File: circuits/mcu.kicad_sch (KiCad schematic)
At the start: 14 parts, among them J1 USB Mini-B, J2 UART->Pi, U10 USBLC6, U11 AP2112K-3.3, U9 ESP32-S3-WROOM-1

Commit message: chore(circuits): update laser controller release artifacts
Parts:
- removed U9: ESP32-S3-WROOM-1, RF_Module:ESP32-S3-WROOM-1, symbol Espressif:ESP32-S3-WROOM-1
- added C29: 1uF, Capacitor_SMD:C_0402_1005Metric_Pad0.74x0.62mm_HandSolder, symbol viv:C_V
- U9: renamed from C29; value 1uF -> ESP32-S3-WROOM-1; footprint Capacitor_SMD:C_0402_1005Metric_Pad0.74x0.62mm_HandSolder -> RF_Module:ESP32-S3-WROOM-1; symbol viv:C_V -> Espressif:ESP32-S3-WROOM-1; LCSC C52923 -> C2913199; Part Number CL05A105KA5NQNC -> ESP32-S3-WROOM-1-N16R8
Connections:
- net +3V3: now also U9.2 (3V3)
- net +5V: now also C29.1; no longer U9.1
- net CONVST: now also U9.10 (GPIO17/U1TXD/ADC2_CH6)
- net ESP_BOOT: now also U9.27 (GPIO0/BOOT)
- net ESP_EN: now also U9.3 (EN)
- net ESP_RX: now also U9.36 (U0RXD/GPIO44/CLK_OUT2)
- net ESP_TX: now also U9.37 (U0TXD/GPIO43/CLK_OUT1)
- net GND: now also U9.1 (GND), U9.40 (GND), U9.41 (GND), C29.2; no longer U9.2
- net ISENSE1: now also U9.4 (GPIO4/TOUCH4/ADC1_CH3)
- net ISENSE2: now also U9.5 (GPIO5/TOUCH5/ADC1_CH4)
- net ISENSE3: now also U9.6 (GPIO6/TOUCH6/ADC1_CH5)
- net ISENSE4: now also U9.7 (GPIO7/TOUCH7/ADC1_CH6)
- net MPD1: now also U9.38 (GPIO2/TOUCH2/ADC1_CH1)
- net MPD2: now also U9.39 (GPIO1/TOUCH1/ADC1_CH0)
- net MPD3: now also U9.12 (GPIO8/TOUCH8/ADC1_CH7/SUBSPICS1)
- net MPD4: now also U9.17 (GPIO9/TOUCH9/ADC1_CH8/FSPIHD/SUBSPIHD)
- net PWM1: now also U9.9 (GPIO16/U0CTS/ADC2_CH5/XTAL_32K_N)
- net PWM2: now also U9.31 (GPIO38/FSPIWP/SUBSPIWP)
- net PWM3: now also U9.21 (GPIO13/TOUCH13/ADC2_CH2/FSPIQ/FSPIIO7/SUBSPIQ)
- net PWM4: now also U9.22 (GPIO14/TOUCH14/ADC2_CH3/FSPIWP/FSPIDQS/SUBSPIWP)
- net USB_DM: now also U9.13 (GPIO19/U1RTS/ADC2_CH8/CLK_OUT2/USB_D-)
- net USB_DP: now also U9.14 (GPIO20/U1CTS/ADC2_CH9/CLK_OUT1/USB_D+)

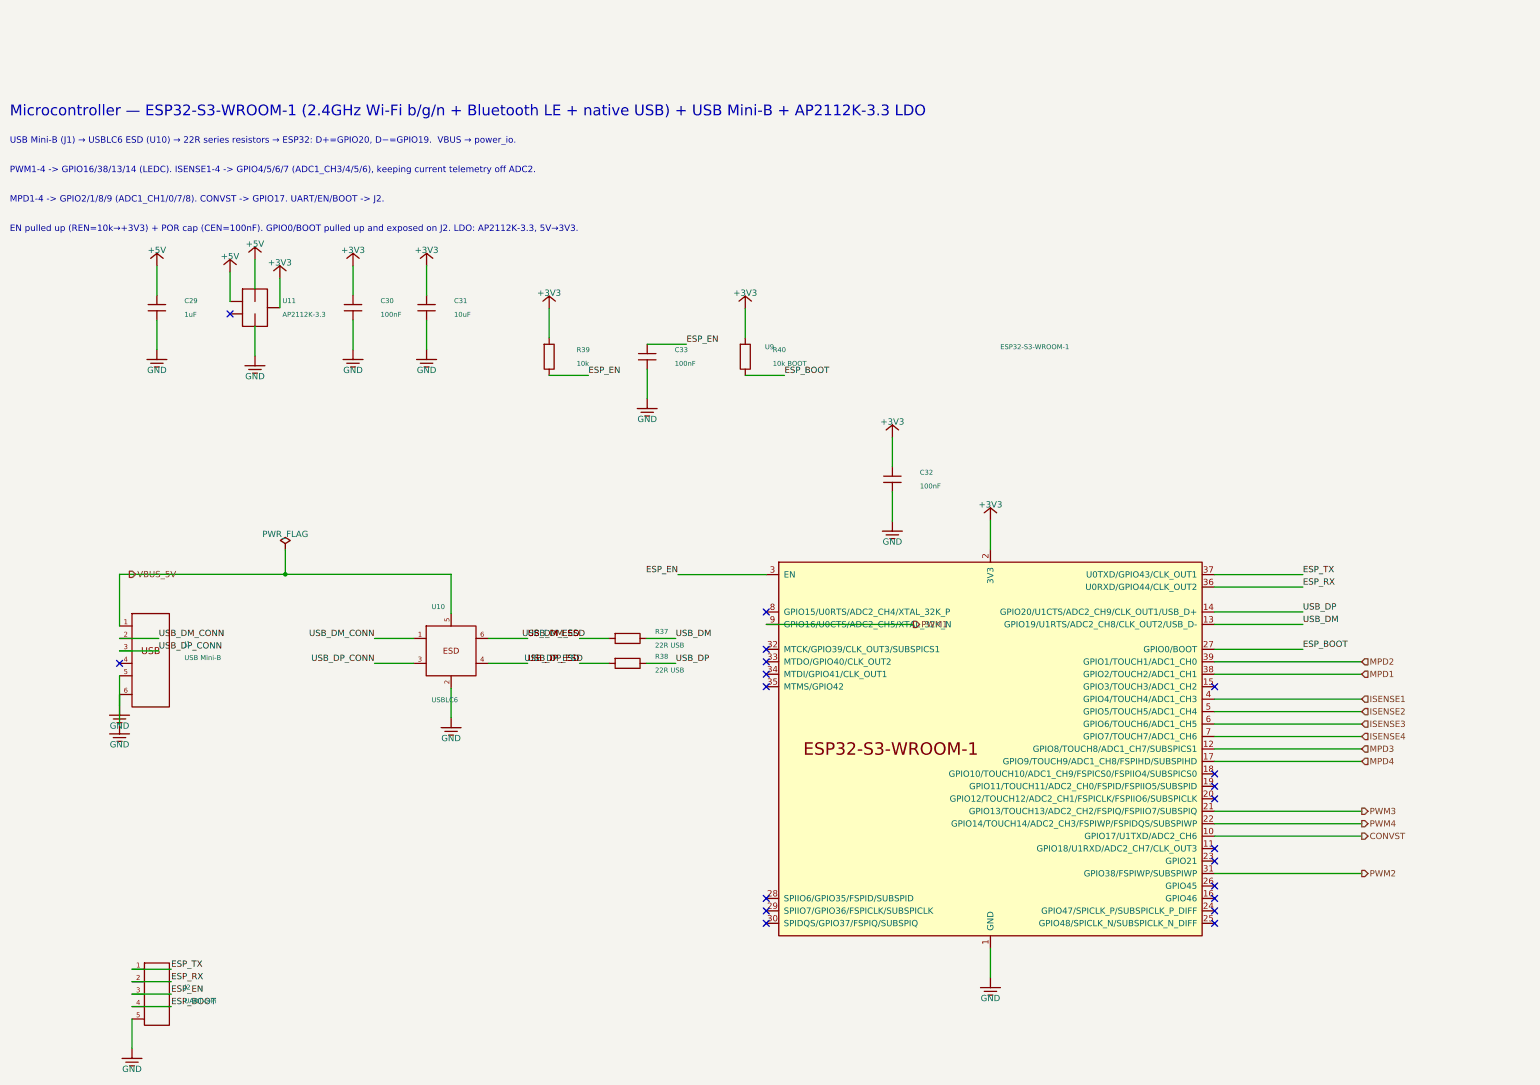
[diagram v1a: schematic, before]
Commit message: fix(circuits): import mcu sheet and laser footprints
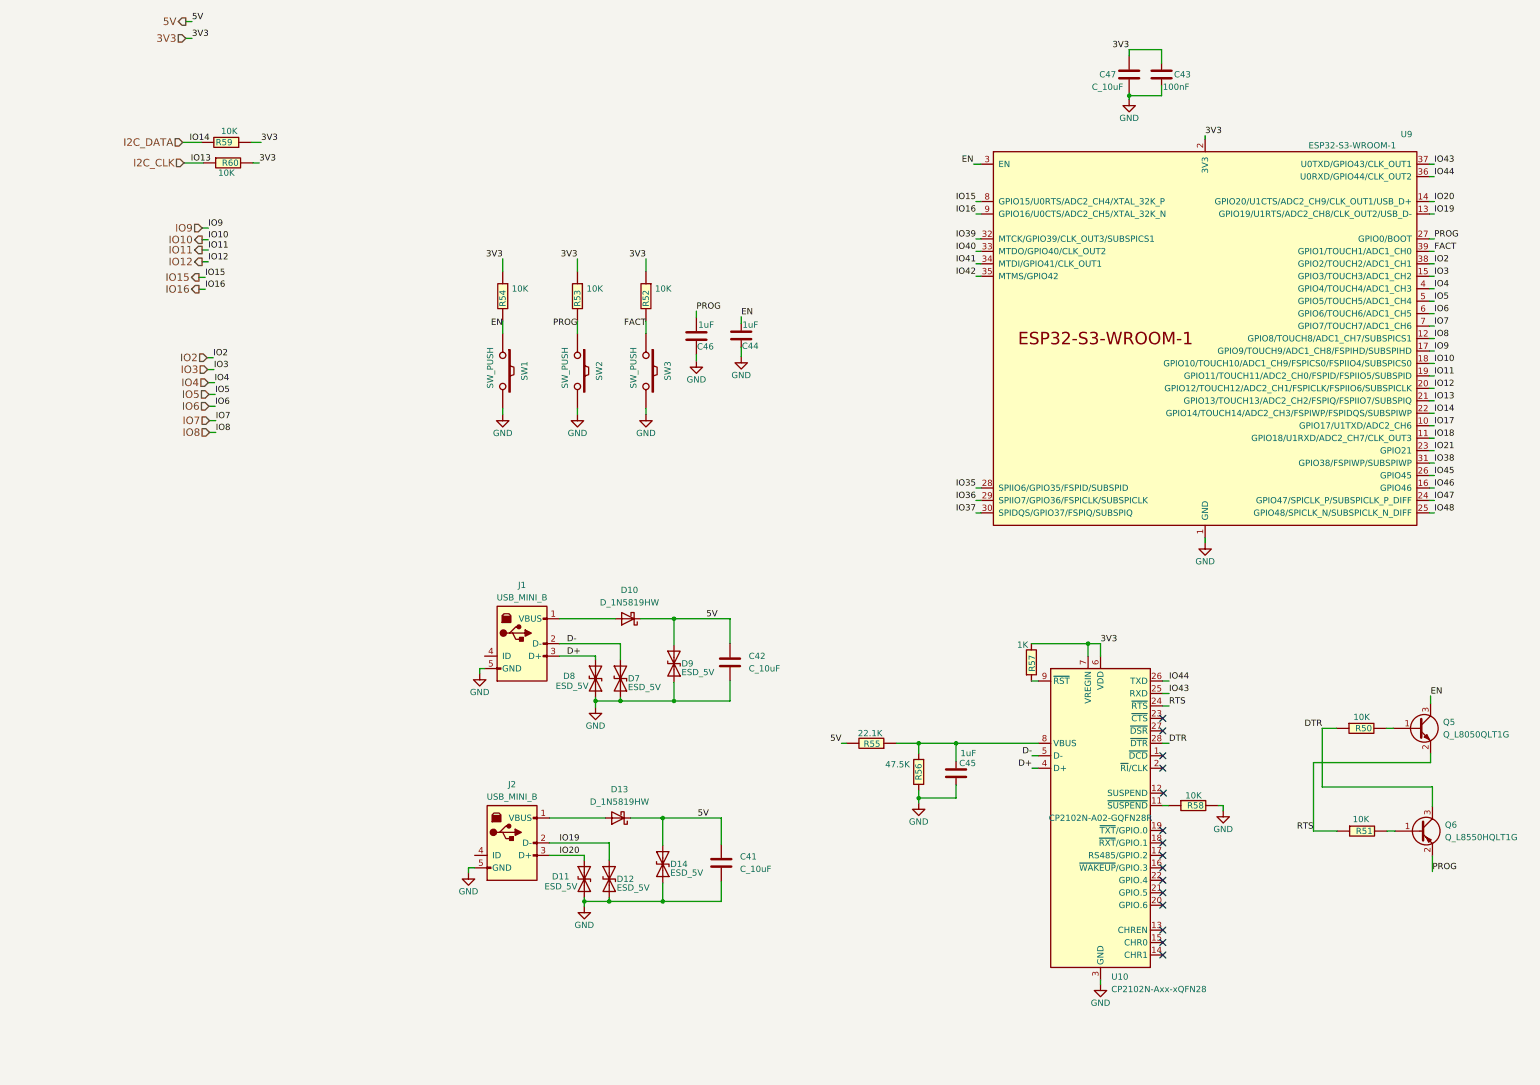
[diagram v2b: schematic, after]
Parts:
- removed C29: 1uF, Capacitor_SMD:C_0402_1005Metric_Pad0.74x0.62mm_HandSolder, symbol viv:C_V
- removed C30, C32, C33: 100nF, Capacitor_SMD:C_0402_1005Metric_Pad0.74x0.62mm_HandSolder, symbol viv:C_V
- removed C31: 10uF, Capacitor_SMD:C_0805_2012Metric_Pad1.18x1.45mm_HandSolder, symbol viv:C_V
- removed J1: USB Mini-B, Connector_USB:USB_Mini-B_Wuerth_65100516121_Horizontal, symbol viv:USB_MINIB
- removed J2: UART->Pi, Connector_PinHeader_2.54mm:PinHeader_1x05_P2.54mm_Vertical, symbol viv:CONN5
- removed R37, R38: 22R USB, Resistor_SMD:R_0603_1608Metric_Pad0.98x0.95mm_HandSolder, symbol viv:R_H
- removed R39: 10k, Resistor_SMD:R_0603_1608Metric_Pad0.98x0.95mm_HandSolder, symbol viv:R_V
- removed R40: 10k BOOT, Resistor_SMD:R_0603_1608Metric_Pad0.98x0.95mm_HandSolder, symbol viv:R_V
- removed U10: USBLC6, Package_TO_SOT_SMD:SOT-23-6, symbol viv:ESD_USB
- removed U11: AP2112K-3.3, Package_TO_SOT_SMD:SOT-23-5, symbol viv:LDO5
- added C41, C42: C_10uF, Capacitor_SMD:C_0805_2012Metric_Pad1.18x1.45mm_HandSolder, symbol open_automation:C_10uF
- added C43: 100nF, Capacitor_SMD:C_0402_1005Metric_Pad0.74x0.62mm_HandSolder, symbol open_automation:C_100nF_0402
- added C44, C45: 1uF, Capacitor_SMD:C_0402_1005Metric_Pad0.74x0.62mm_HandSolder, symbol open_automation:C_1uF
- added C46: 1uF, Capacitor_SMD:C_0402_1005Metric_Pad0.74x0.62mm_HandSolder, symbol Open_Automation:C_1uF
- added C47: C_10uF, Capacitor_SMD:C_0805_2012Metric_Pad1.18x1.45mm_HandSolder, symbol Open_Automation:C_10uF
- added D10, D13: D_1N5819HW, Diode_SMD:D_SOD-123, symbol open_automation:D_1N5819HW
- added D11, D12, D14, D7, D8, D9: ESD_5V, Diode_SMD:D_SOD-523, symbol open_automation:D_ESD9B5.0ST5G
- added J1, J2: USB_MINI_B, Connector_USB:USB_Mini-B_Wuerth_65100516121_Horizontal, symbol open_automation:USB_MINI_B_SMD
- added Q5: Q_L8050QLT1G, Package_TO_SOT_SMD:SOT-23, symbol open_automation:Q_L8050QLT1G
- added Q6: Q_L8550HQLT1G, Package_TO_SOT_SMD:SOT-23, symbol open_automation:Q_L8550HQLT1G
- added R50, R51, R52, R53, R54, R58, R59, R60: 10K, Resistor_SMD:R_0402_1005Metric_Pad0.72x0.64mm_HandSolder, symbol Open_Automation:R_10K_0402
- added R55: 22.1K, Resistor_SMD:R_0402_1005Metric_Pad0.72x0.64mm_HandSolder, symbol open_automation:R_22.1K_0402
- added R56: 47.5K, Resistor_SMD:R_0603_1608Metric_Pad0.98x0.95mm_HandSolder, symbol open_automation:R_47.5k
- added R57: 1K, Resistor_SMD:R_0402_1005Metric_Pad0.72x0.64mm_HandSolder, symbol open_automation:R_1K_0402
- added SW1, SW2, SW3: SW_PUSH, Button_Switch_SMD:SW_SPST_PTS645, symbol open-dash-daughterboard-rescue:SW_PUSH-Open_Automation
- added U10: CP2102N-Axx-xQFN28, Package_DFN_QFN:QFN-28-1EP_5x5mm_P0.5mm_EP3.35x3.35mm, symbol Interface_USB:CP2102N-Axx-xQFN28
- U9: footprint RF_Module:ESP32-S3-WROOM-1 -> Espressif:ESP32-S3-WROOM-1; Part Number ESP32-S3-WROOM-1-N16R8 -> ESP32-S3-WROOM-1-N16
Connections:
- net GND: now also C41.2, C42.2, C43.2, C44.2, C45.2, C46.2, C47.2, D11.1 (A1), D12.1 (A1), D14.1 (A1), D7.1 (A1), D8.1 (A1), D9.1 (A1), J1.5 (GND), J2.5 (GND), R56.1, R58.2, SW1.2, SW2.2, SW3.2, U10.29 (GND), U10.3 (GND)
- net IO18: now reaches U9.11 (GPIO18/U1RXD/ADC2_CH7/CLK_OUT3)
- net IO3: now reaches U9.15 (GPIO3/TOUCH3/ADC1_CH2)
- net IO46: now reaches U9.16 (GPIO46)
- net IO10: now reaches U9.18 (GPIO10/TOUCH10/ADC1_CH9/FSPICS0/FSPIIO4/SUBSPICS0)
- net IO11: now reaches U9.19 (GPIO11/TOUCH11/ADC2_CH0/FSPID/FSPIIO5/SUBSPID)
- net IO12: now reaches U9.20 (GPIO12/TOUCH12/ADC2_CH1/FSPICLK/FSPIIO6/SUBSPICLK)
- net IO21: now reaches U9.23 (GPIO21)
- net IO47: now reaches U9.24 (GPIO47/SPICLK_P/SUBSPICLK_P_DIFF)
- net IO48: now reaches U9.25 (GPIO48/SPICLK_N/SUBSPICLK_N_DIFF)
- net IO45: now reaches U9.26 (GPIO45)
- net IO35: now reaches U9.28 (SPIIO6/GPIO35/FSPID/SUBSPID)
- net IO36: now reaches U9.29 (SPIIO7/GPIO36/FSPICLK/SUBSPICLK)
- net IO37: now reaches U9.30 (SPIDQS/GPIO37/FSPIQ/SUBSPIQ)
- net IO39: now reaches U9.32 (MTCK/GPIO39/CLK_OUT3/SUBSPICS1)
- net IO40: now reaches U9.33 (MTDO/GPIO40/CLK_OUT2)
- net IO41: now reaches U9.34 (MTDI/GPIO41/CLK_OUT1)
- net IO42: now reaches U9.35 (MTMS/GPIO42)
- net IO15: now reaches U9.8 (GPIO15/U0RTS/ADC2_CH4/XTAL_32K_P)
- net +3V3 renamed 3V3
- net 3V3: now also C43.1, C47.1, R52.1, R53.1, R54.1, R57.1, R59.1, R60.2, U10.6 (VDD), U10.7 (VREGIN)
- net CONVST renamed IO17
- net ESP_BOOT renamed PROG
- net PROG: now also C46.1, Q6.2 (E), R53.2, SW2.1
- net ESP_EN renamed EN
- net EN: now also C44.1, Q5.3 (C), R54.2, SW1.1
- net ESP_RX renamed IO44
- net IO44: now also U10.26 (TXD)
- net ESP_TX renamed IO43
- net IO43: now also U10.25 (RXD)
- net ISENSE1 renamed IO4
- net ISENSE2 renamed IO5
- net ISENSE3 renamed IO6
- net ISENSE4 renamed IO7
- net MPD1 renamed IO2
- net MPD2 renamed FACT
- net FACT: now also R52.2, SW3.1
- net MPD3 renamed IO8
- net MPD4 renamed IO9
- net PWM1 renamed IO16
- net PWM2 renamed IO38
- net PWM3 renamed I2C_CLK
- net I2C_CLK: now also R60.1
- net PWM4 renamed I2C_DATA
- net I2C_DATA: now also R59.2
- net USB_DM renamed IO19
- net IO19: now also D12.2 (A2), J2.2 (D-)
- net USB_DP renamed IO20
- net IO20: now also D11.2 (A2), J2.3 (D+)
- new net: C45.1, R55.1, R56.2, U10.8 (VBUS)
- new net: D13.2 (A), J2.1 (VBUS)
- new net: R57.2, U10.9 (~{RST})
- new net: R58.1, U10.11 (~{SUSPEND})
- new net: Q5.1 (B), R50.2
- new net: D10.2 (A), J1.1 (VBUS)
- new net: Q6.1 (B), R51.2
- new net 5V: C41.1, C42.1, D10.1 (K), D13.1 (K), D14.2 (A2), D9.2 (A2), R55.2
- new net D+: D8.2 (A2), J1.3 (D+), U10.4 (D+)
- new net D-: D7.2 (A2), J1.2 (D-), U10.5 (D-)
- new net DTR: Q6.3 (C), R50.1, U10.28 (~{DTR})
- new net RTS: Q5.2 (E), R51.1, U10.24 (~{RTS})
- no-connect marks 20 -> 15
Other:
- note removed: "EN pulled up (REN=10k→+3V3) + POR cap (CEN=100nF). GPIO0/BOOT pulled up and exposed on J2. LDO: AP2112K-3.3, 5V→3V3."
- note removed: "MPD1-4 -> GPIO2/1/8/9 (ADC1_CH1/0/7/8). CONVST -> GPIO17. UART/EN/BOOT -> J2."
- note removed: "Microcontroller — ESP32-S3-WROOM-1 (2.4GHz Wi-Fi b/g/n + Bluetooth LE + native USB) + USB Mini-B + AP2112K-3.3 LDO"
- note removed: "PWM1-4 -> GPIO16/38/13/14 (LEDC). ISENSE1-4 -> GPIO4/5/6/7 (ADC1_CH3/4/5/6), keeping current telemetry off ADC2."
- note removed: "USB Mini-B (J1) → USBLC6 ESD (U10) → 22R series resistors → ESP32: D+=GPIO20, D−=GPIO19. VBUS → power_io."
- company: Vivonics -> (none)
- title: Microcontroller -> (none)

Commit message: save current laser controller recovery state
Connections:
- net GND: now also J1.6 (GND), J2.6 (GND)
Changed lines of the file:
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@@
+    (stroke (width 0) (type default))
+  )
+  (wire (pts (xy 124.3076 163.6014) (xy 125.8316 163.6014))
     (stroke (width 0) (type default))
   )
@@
   )
   (wire (pts (xy 123.5456 204.2414) (xy 124.8156 204.2414))
+    (stroke (width 0) (type default))
+  )
+  (wire (pts (xy 122.2756 204.2414) (xy 123.5456 204.2414))
     (stroke (width 0) (type default))
   )
@@
     (pin "4")
     (pin "5")
+    (pin "6")
     (instances
       (project "thermostat"
@@
     (pin "4")
     (pin "5")
-    (instances
-      (project "thermostat"
+    (pin "6")
+    (instances
+      (project "thermostat"
